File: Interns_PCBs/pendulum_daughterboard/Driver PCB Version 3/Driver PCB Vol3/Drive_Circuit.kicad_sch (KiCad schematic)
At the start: 12 parts, among them IC5 MAX9928FAUA+, J2 Coil, Q1 BC557, Q2 BC547

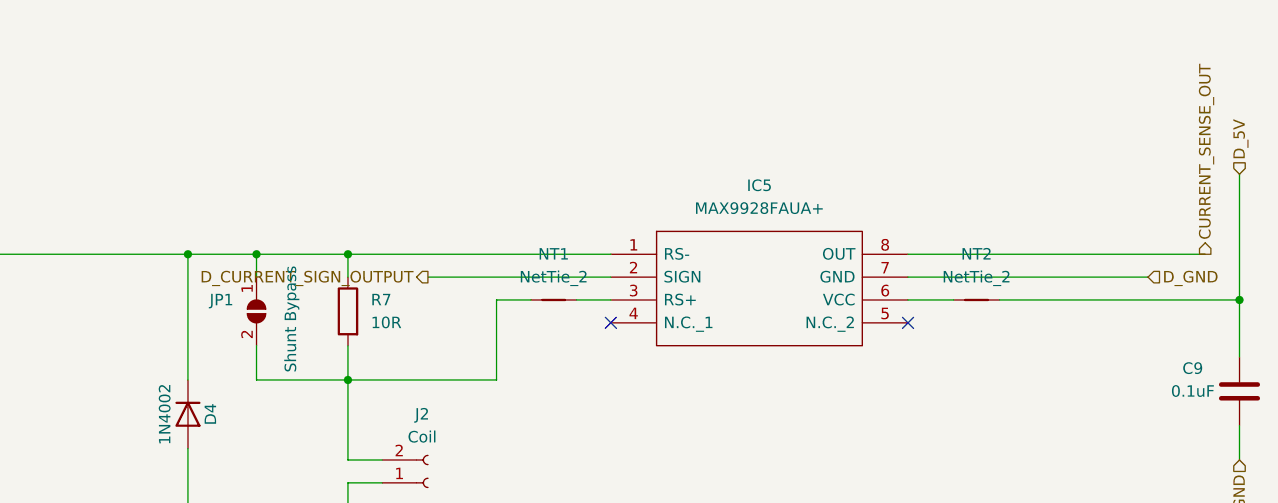
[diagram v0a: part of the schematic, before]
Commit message: Flipped Diode on schematic
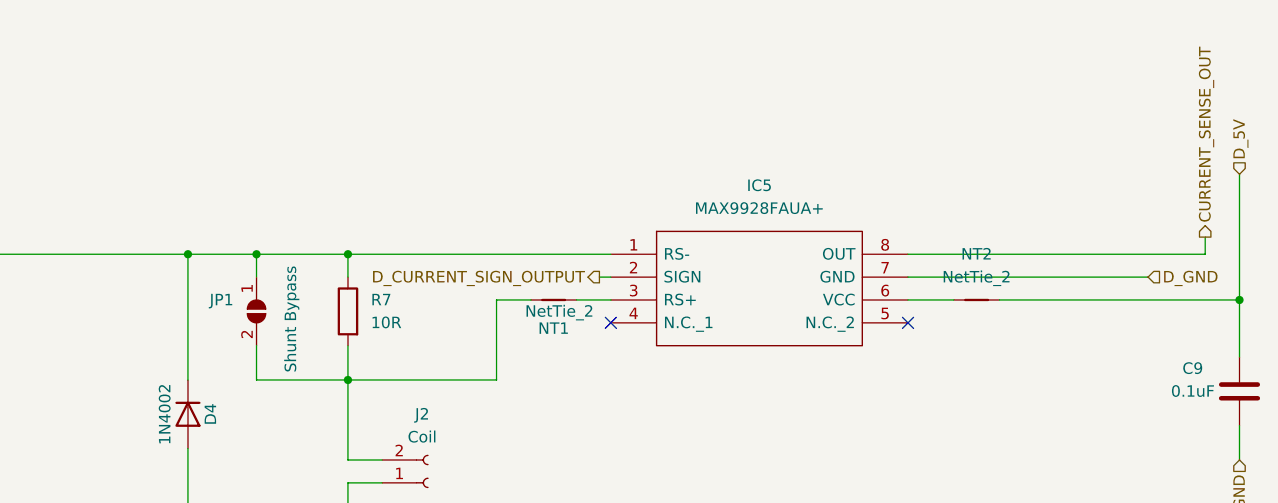
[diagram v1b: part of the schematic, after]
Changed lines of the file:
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@@
+    (stroke (width 0) (type default) (color 0 0 0 0))
+  )
+  (wire (pts (xy 275.59 73.025) (xy 275.59 74.93))
     (stroke (width 0) (type default) (color 0 0 0 0))
   )
@@
     (stroke (width 0) (type default) (color 0 0 0 0))
   )
-  (wire (pts (xy 189.23 77.47) (xy 209.55 77.47))
+  (wire (pts (xy 208.28 77.47) (xy 209.55 77.47))
     (stroke (width 0) (type default) (color 0 0 0 0))
   )
@@
     (effects (font (size 1.27 1.27)) (justify left))
   )
+  (hierarchical_label "CURRENT_SENSE_OUT" (shape output) (at 275.59 73.025 90)
+    (effects (font (size 1.27 1.27)) (justify left))
+  )
   (hierarchical_label "LOAD_MCU" (shape input) (at 72.39 91.44 180)
     (effects (font (size 1.27 1.27)) (justify right))
@@
     (effects (font (size 1.27 1.27)) (justify right))
   )
-  (hierarchical_label "D_CURRENT_SIGN_OUTPUT" (shape output) (at 189.23 77.47 180)
+  (hierarchical_label "D_CURRENT_SIGN_OUTPUT" (shape output) (at 208.28 77.47 180)
     (effects (font (size 1.27 1.27)) (justify right))
   )
   (hierarchical_label "DRIVE_5V" (shape input) (at 66.04 74.93 90)
-    (effects (font (size 1.27 1.27)) (justify left))
-  )
-  (hierarchical_label "CURRENT_SENSE_OUT" (shape output) (at 275.59 74.93 90)
     (effects (font (size 1.27 1.27)) (justify left))
   )
@@
   )
   (symbol (lib_id "Device:NetTie_2") (at 203.2 80.01 0) (unit 1)
-    (in_bom yes) (on_board yes) (fields_autoplaced)
-    (property "Reference" "NT1" (id 0) (at 203.2 74.93 0))
-    (property "Value" "NetTie_2" (id 1) (at 203.2 77.47 0))
+    (in_bom yes) (on_board yes)
+    (property "Reference" "NT1" (id 0) (at 203.2 83.185 0))
+    (property "Value" "NetTie_2" (id 1) (at 203.835 81.28 0))
     (property "Footprint" "NetTie:NetTie-2_SMD_Pad0.5mm" (id 2) (at 203.2 80.01 0)
       (effects (font (size 1.27 1.27)) hide)
